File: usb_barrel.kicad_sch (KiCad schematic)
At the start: 11 parts, among them J1 BarrelJack_3167288, J2 USB4105-GF-A, U2 AP62301Z6-7

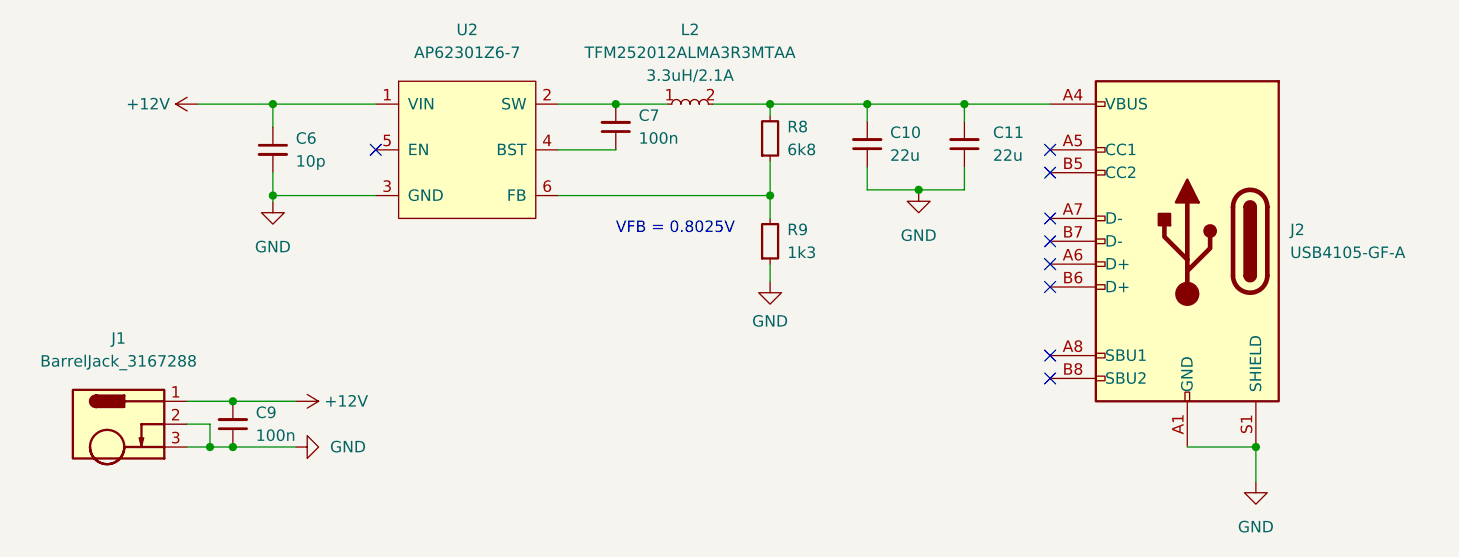
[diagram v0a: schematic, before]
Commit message: Added pull down resistors on USB
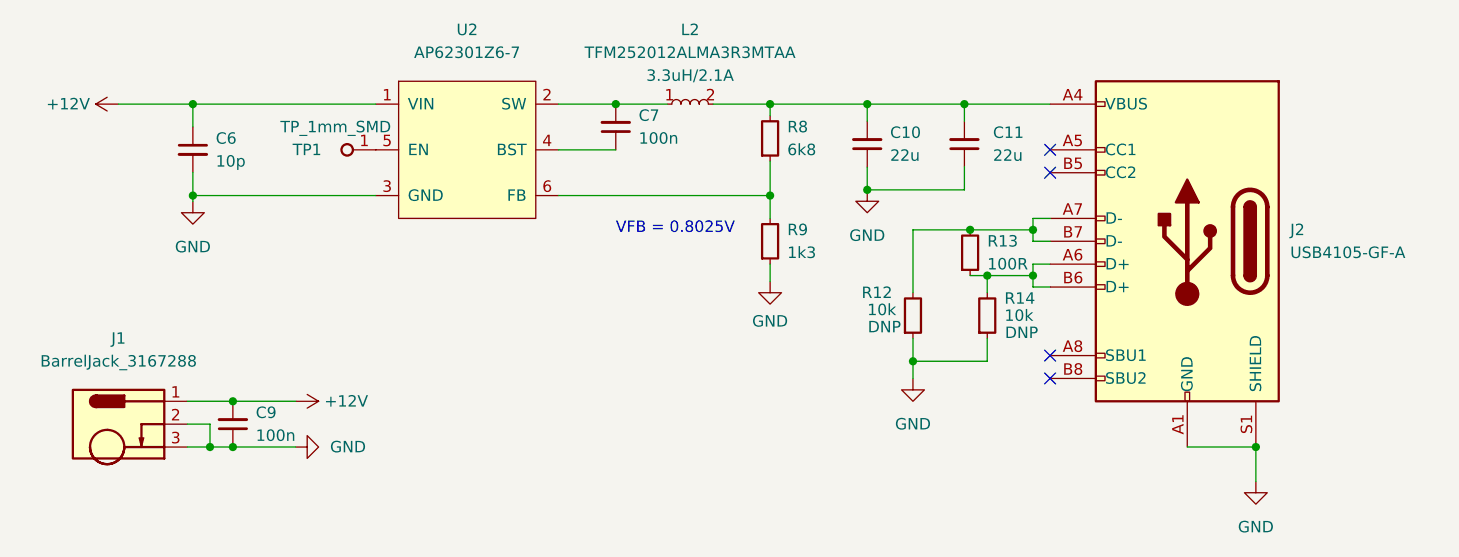
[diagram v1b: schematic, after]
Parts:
- added R12, R14: R_10k_0402, antmicro-footprints:R_0402_1005Metric, symbol antmicroResistors0402:R_10k_0402
- added R13: R_100R_0402, antmicro-footprints:R_0402_1005Metric, symbol antmicroResistors0402:R_100R_0402
- added TP1: TP_1mm_SMD, antmicro-footprints:TP_SMD_1_MM, symbol antmicroTestPoints:TP_1mm_SMD
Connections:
- net GND: now also R12.1, R14.1
- net at J2.A6 (D+): now also J2.B6 (D+), R13.1, R14.2
- net at J2.A7 (D-): now also J2.B7 (D-), R12.2, R13.2
- net at U2.5 (EN): now also TP1.1
- no-connect marks 9 -> 4
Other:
- moved on the sheet: C6
